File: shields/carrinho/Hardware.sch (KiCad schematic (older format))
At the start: 78 parts, among them J1 Conn_02x02_Odd_Even, J10 Conn_01x04, J11 Conn_01x04, J12 Conn_02x13_Odd_Even, J2 Conn_01x04, J3 Conn_02x02_Odd_Even, J4 Conn_01x02_Male, J5 Conn_01x02_Male, J6 Conn_01x02_Male, J7 Conn_01x02_Male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

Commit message: Improved schematic
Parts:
- C3: value C -> 100n
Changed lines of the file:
@@
 EESchema Schematic File Version 4
 LIBS:Hardware-cache
-EELAYER 30 0
+EELAYER 26 0
 EELAYER END
 $Descr A4 11693 8268
@@
 U 1 1 5CBBCEEC
 P 1300 5500
-F 0 "R14" H 1093 5500 50  0000 C CNN
-F 1 "15k" V 1184 5500 50  0000 C CNN
+F 0 "R14" V 1500 5500 50  0000 C CNN
+F 1 "15k" V 1400 5500 50  0000 C CNN
 F 2 "Resistor_SMD:R_0805_2012Metric" V 1230 5500 50  0001 C CNN
 F 3 "~" H 1300 5500 50  0001 C CNN
@@
 P 1300 5300
 F 0 "R12" V 1093 5300 50  0000 C CNN
-F 1 "15k" V 1184 5300 50  0000 C CNN
+F 1 "15k" V 1200 5300 50  0000 C CNN
 F 2 "Resistor_SMD:R_0805_2012Metric" V 1230 5300 50  0001 C CNN
 F 3 "~" H 1300 5300 50  0001 C CNN
@@
 P 3050 5400
 F 0 "#PWR017" H 3050 5250 50  0001 C CNN
-F 1 "+BATT" H 3065 5573 50  0000 C CNN
+F 1 "+BATT" H 2900 5350 50  0000 C CNN
 F 2 "" H 3050 5400 50  0001 C CNN
 F 3 "" H 3050 5400 50  0001 C CNN
@@
 U 1 1 5CC0410F
 P 3200 5450
-F 0 "R13" H 2993 5450 50  0000 C CNN
-F 1 "30k" V 3084 5450 50  0000 C CNN
+F 0 "R13" V 3400 5450 50  0000 C CNN
+F 1 "30k" V 3300 5450 50  0000 C CNN
 F 2 "Resistor_SMD:R_0805_2012Metric" V 3130 5450 50  0001 C CNN
 F 3 "~" H 3200 5450 50  0001 C CNN
@@
 U 1 1 5CC04116
 P 3200 5250
-F 0 "R11" V 2993 5250 50  0000 C CNN
-F 1 "30k" V 3084 5250 50  0000 C CNN
+F 0 "R11" V 3000 5250 50  0000 C CNN
+F 1 "30k" V 3100 5250 50  0000 C CNN
 F 2 "Resistor_SMD:R_0805_2012Metric" V 3130 5250 50  0001 C CNN
 F 3 "~" H 3200 5250 50  0001 C CNN
@@
 Text Notes 6500 2650 0    79   ~ 0
 Ponte H Lado esquerdo\n
-Text Notes 800  4700 0    79   ~ 0
+Text Notes 800  4650 0    79   ~ 0
 Diferencial bateria
 Wire Notes Line
@@
 U 1 1 5CE81B2B
 P 8900 5650
-F 0 "RV2" H 8830 5696 50  0000 R CNN
-F 1 "R_POT_TRIM" H 8830 5605 50  0000 R CNN
+F 0 "RV2" H 8800 5550 50  0000 R CNN
+F 1 "R_POT_TRIM" H 8800 5450 50  0000 R CNN
 F 2 "Potentiometer_THT:Potentiometer_Piher_PT-10-H01_Horizontal" H 8900 5650 50  0001 C CNN
 F 3 "~" H 8900 5650 50  0001 C CNN
@@
 U 2 1 5CF27E4C
 P 10250 5550
-F 0 "U1" H 10250 5917 50  0000 C CNN
-F 1 "LM393" H 10250 5826 50  0000 C CNN
+F 0 "U1" H 10150 5900 50  0000 C CNN
+F 1 "LM393" H 10200 5800 50  0000 C CNN
 F 2 "" H 10250 5550 50  0001 C CNN
 F 3 "http://www.ti.com/lit/ds/symlink/lm393-n.pdf" H 10250 5550 50  0001 C CNN
@@
 U 1 1 5CF855F3
 P 10650 5250
-F 0 "D10" V 10688 5133 50  0000 R CNN
+F 0 "D10" V 10700 5100 50  0000 R CNN
 F 1 "LED" V 10597 5133 50  0000 R CNN
 F 2 "LED_SMD:LED_0805_2012Metric" H 10650 5250 50  0001 C CNN
@@
 U 1 1 5CFF8CA7
 P 6550 5650
-F 0 "RV1" H 6480 5696 50  0000 R CNN
-F 1 "R_POT_TRIM" H 6480 5605 50  0000 R CNN
+F 0 "RV1" H 6450 5600 50  0000 R CNN
+F 1 "R_POT_TRIM" H 6500 5450 50  0000 R CNN
 F 2 "Potentiometer_THT:Potentiometer_Piher_PT-10-H01_Horizontal" H 6550 5650 50  0001 C CNN
 F 3 "~" H 6550 5650 50  0001 C CNN
@@
 U 3 1 5D0103DD
 P 6050 5500
-F 0 "U1" H 6008 5546 50  0000 L CNN
-F 1 "LM393" H 6008 5455 50  0000 L CNN
+F 0 "U1" H 5700 5600 50  0000 L CNN
+F 1 "LM393" H 5650 5500 50  0000 L CNN
 F 2 "" H 6050 5500 50  0001 C CNN
 F 3 "http://www.ti.com/lit/ds/symlink/lm393-n.pdf" H 6050 5500 50  0001 C CNN
@@
 	11100 4500 5800 4500
 Wire Notes Line
-	5800 4500 5800 6450
-Wire Notes Line
-	5800 6450 11100 6450
+	5650 4500 5650 6450
+Wire Notes Line
+	5650 6450 10950 6450
 Wire Notes Line
 	11100 6450 11100 4500
@@
 U 1 1 5D4E9A1A
 P 10550 5250
-F 0 "R34" H 10620 5296 50  0000 L CNN
-F 1 "10k" H 10620 5205 50  0000 L CNN
+F 0 "R34" H 10350 5400 50  0000 L CNN
+F 1 "10k" H 10350 5300 50  0000 L CNN
 F 2 "Resistor_SMD:R_0805_2012Metric_Pad1.15x1.40mm_HandSolder" V 10480 5250 50  0001 C CNN
 F 3 "~" H 10550 5250 50  0001 C CNN
@@
 U 1 1 5CBB5DEC
 P 1900 5400
-F 0 "U3" H 1900 5033 50  0000 C CNN
-F 1 "LM324" H 1900 5124 50  0000 C CNN
+F 0 "U3" H 1900 5100 50  0000 C CNN
+F 1 "LM324" H 1950 5200 50  0000 C CNN
 F 2 "Package_SO:SOIC-14_3.9x8.7mm_P1.27mm" H 1850 5500 50  0001 C CNN
 F 3 "http://www.ti.com/lit/ds/symlink/lm2902-n.pdf" H 1950 5600 50  0001 C CNN
@@
 P 6150 5500
 F 0 "C3" H 6265 5546 50  0000 L CNN
-F 1 "C" H 6265 5455 50  0000 L CNN
+F 1 "100n" H 6265 5455 50  0000 L CNN
 F 2 "Capacitor_SMD:C_0805_2012Metric" H 6188 5350 50  0001 C CNN
 F 3 "~" H 6150 5500 50  0001 C CNN

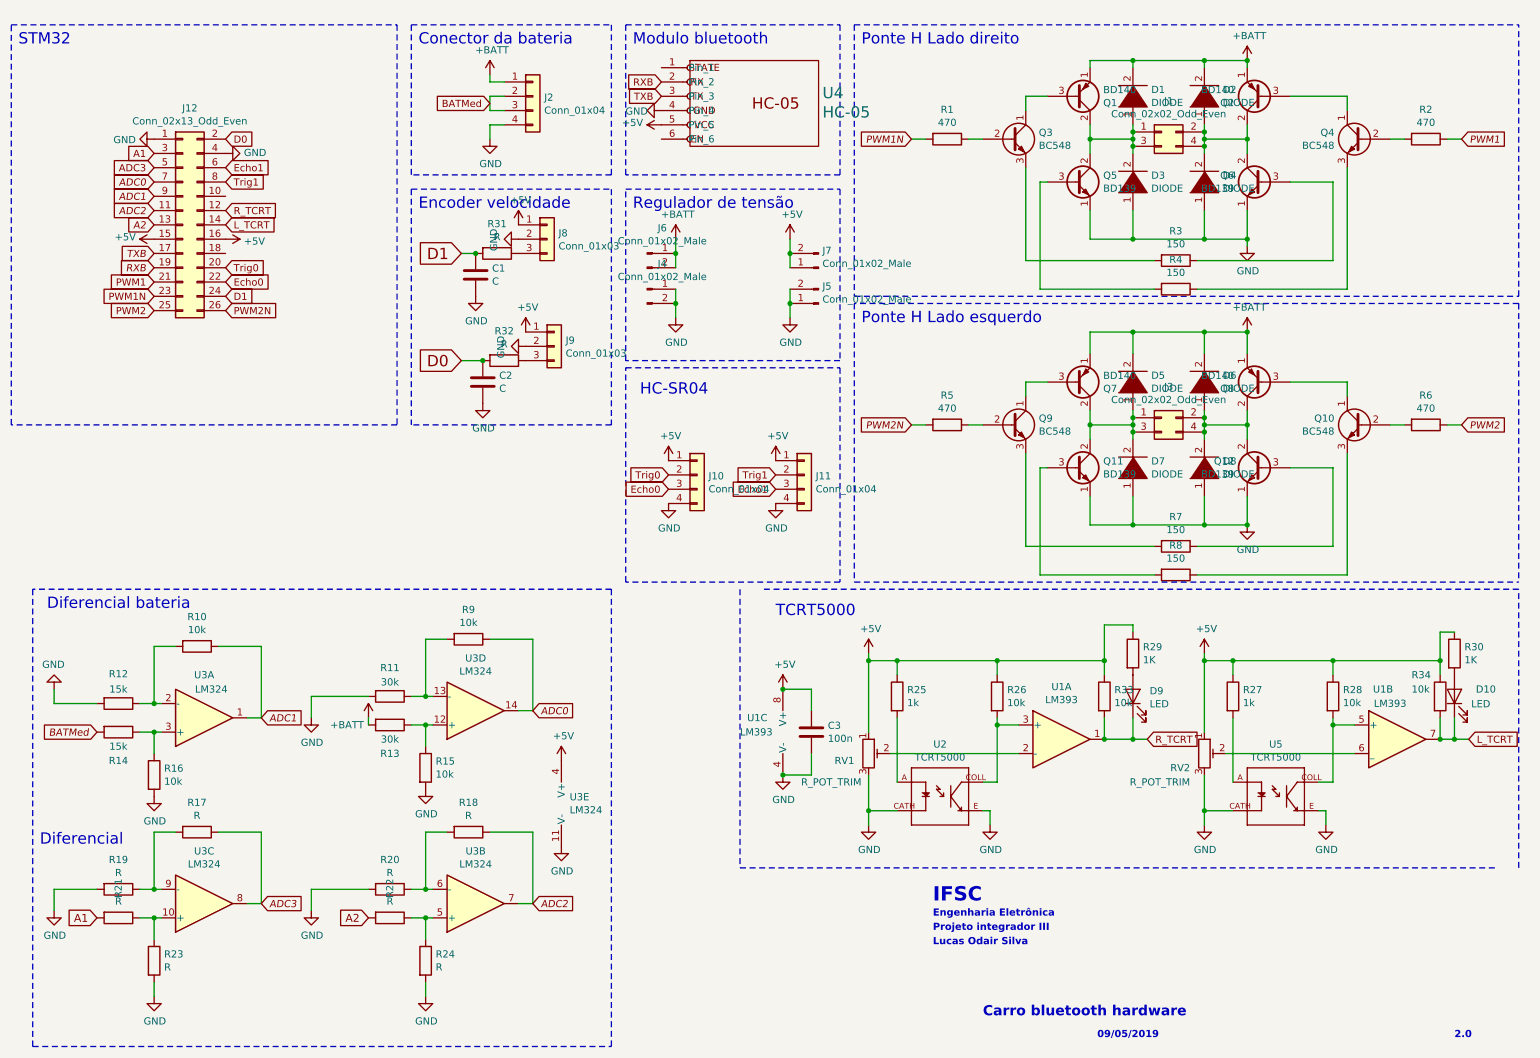
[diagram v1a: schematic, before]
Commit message: Changed motors conector, added capacitor near ampop
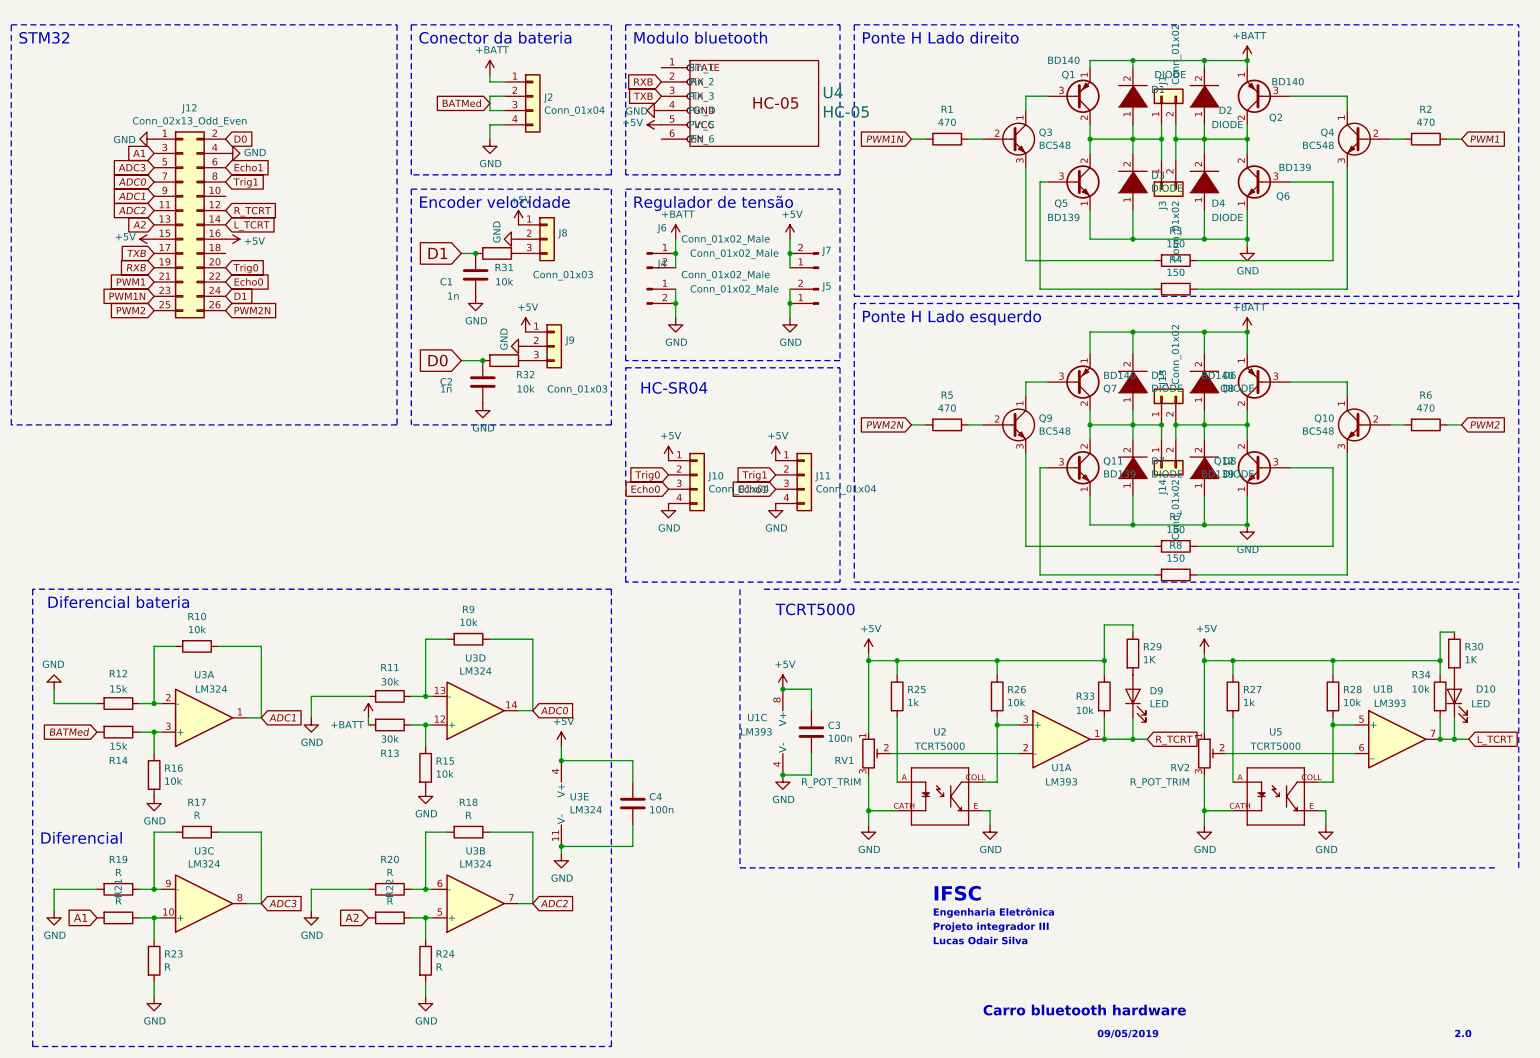
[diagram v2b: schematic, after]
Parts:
- removed J1, J3: Conn_02x02_Odd_Even, Connector_PinHeader_2.54mm:PinHeader_2x02_P2.54mm_Vertical, symbol Connector_Generic:Conn_02x02_Odd_Even
- added C4: 100n, Capacitor_SMD:C_0805_2012Metric, symbol Device:C
- added J1, J13, J14, J3: Conn_01x02, Connector_PinHeader_2.54mm:PinHeader_1x02_P2.54mm_Vertical, symbol Connector_Generic:Conn_01x02
- C1, C2: value C -> 1n
- R31, R32: value R -> 10k
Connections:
- net +5V: now also C4.1
- net GND: now also C4.2
- net at D1.1 (K), D3.2 (A), Q1.2 (C)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: now also J1.1 (Pin_1), J3.1 (Pin_1)
- net at D2.1 (K), D4.2 (A), Q2.2 (C)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: now also J1.2 (Pin_2), J3.2 (Pin_2)
- net at D5.1 (K), D7.2 (A), Q11.2 (C)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: now also J13.1 (Pin_1), J14.1 (Pin_1)
- net at D6.1 (K), D8.2 (A), Q12.2 (C)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: now also J13.2 (Pin_2), J14.2 (Pin_2)

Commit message: Changed pots
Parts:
- RV1, RV2: footprint Potentiometer_THT:Potentiometer_Piher_PT-10-H01_Horizontal -> Potentiometer_THT:Potentiometer_Piher_PT-6-V_Vertical
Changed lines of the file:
@@
 F 0 "RV2" H 8800 5550 50  0000 R CNN
 F 1 "R_POT_TRIM" H 8800 5450 50  0000 R CNN
-F 2 "Potentiometer_THT:Potentiometer_Piher_PT-10-H01_Horizontal" H 8900 5650 50  0001 C CNN
+F 2 "Potentiometer_THT:Potentiometer_Piher_PT-6-V_Vertical" H 8900 5650 50  0001 C CNN
 F 3 "~" H 8900 5650 50  0001 C CNN
 	1    8900 5650
@@
 F 0 "RV1" H 6450 5600 50  0000 R CNN
 F 1 "R_POT_TRIM" H 6500 5450 50  0000 R CNN
-F 2 "Potentiometer_THT:Potentiometer_Piher_PT-10-H01_Horizontal" H 6550 5650 50  0001 C CNN
+F 2 "Potentiometer_THT:Potentiometer_Piher_PT-6-V_Vertical" H 6550 5650 50  0001 C CNN
 F 3 "~" H 6550 5650 50  0001 C CNN
 	1    6550 5650

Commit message: Updated car PCB
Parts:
- added D11: LED, LED_SMD:LED_0805_2012Metric, symbol Device:LED
- added D12: D_Schottky, Diode_SMD:D_SMB, symbol Device:D_Schottky
- added H1, H2, H3: MountingHole, MountingHole:MountingHole_3.2mm_M3, symbol Mechanical:MountingHole
- added R35: 1K, Resistor_SMD:R_0805_2012Metric, symbol Device:R
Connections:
- net +5V: now also D11.2 (A)
- net +BATT: now also D12.1 (K); no longer J2.1 (Pin_1)
- net GND: now also R35.2
- new net: D12.2 (A), J2.1 (Pin_1)
- new net: D11.1 (K), R35.1
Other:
- note added: "Controll conector"
- note removed: "STM32"
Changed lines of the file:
@@
 L power:+BATT #PWR06
 U 1 1 5CBAF568
-P 3900 900
-F 0 "#PWR06" H 3900 750 50  0001 C CNN
-F 1 "+BATT" H 3915 1073 50  0000 C CNN
-F 2 "" H 3900 900 50  0001 C CNN
-F 3 "" H 3900 900 50  0001 C CNN
-	1    3900 900
-	1    0    0    -1
-$EndComp
-Wire Wire Line
-	3900 900  3900 950
-Wire Wire Line
-	3900 950  4000 950
+P 3450 950
+F 0 "#PWR06" H 3450 800 50  0001 C CNN
+F 1 "+BATT" H 3465 1123 50  0000 C CNN
+F 2 "" H 3450 950 50  0001 C CNN
+F 3 "" H 3450 950 50  0001 C CNN
+	1    3450 950
+	1    0    0    -1
+$EndComp
 Wire Wire Line
 	4000 1050 3900 1050
@@
 Wire Notes Line
 	4850 1700 6350 1700
-Text Notes 4900 1850 0    79   ~ 0
+Text Notes 4950 1850 0    79   ~ 0
 Regulador de tensão
 Wire Notes Line
@@
 	550  550  3250 550
 Text Notes 600  700  0    79   ~ 0
-STM32
+Controll conector
 $Comp
 L power:+5V #PWR0101
@@
 L power:+BATT #PWR02
 U 1 1 5CC49D66
-P 5200 2050
-F 0 "#PWR02" H 5200 1900 50  0001 C CNN
-F 1 "+BATT" H 5215 2223 50  0000 C CNN
-F 2 "" H 5200 2050 50  0001 C CNN
-F 3 "" H 5200 2050 50  0001 C CNN
-	1    5200 2050
+P 5200 2000
+F 0 "#PWR02" H 5200 1850 50  0001 C CNN
+F 1 "+BATT" H 5050 2050 50  0000 C CNN
+F 2 "" H 5200 2000 50  0001 C CNN
+F 3 "" H 5200 2000 50  0001 C CNN
+	1    5200 2000
 	1    0    0    -1
 $EndComp
@@
 U 1 1 5CEE1749
 P 5000 2400
-F 0 "J4" H 5106 2578 50  0000 C CNN
-F 1 "Conn_01x02_Male" H 5550 2500 50  0000 C CNN
+F 0 "J4" H 5000 2200 50  0000 C CNN
+F 1 "Conn_01x02_Male" H 5550 2100 50  0000 C CNN
 F 2 "Connector_PinSocket_2.54mm:PinSocket_1x02_P2.54mm_Vertical" H 5000 2400 50  0001 C CNN
 F 3 "~" H 5000 2400 50  0001 C CNN
@@
 P 6200 2500
 F 0 "J5" H 6173 2380 50  0000 R CNN
-F 1 "Conn_01x02_Male" H 7100 2400 50  0000 R CNN
+F 1 "Conn_01x02_Male" H 7100 2800 50  0000 R CNN
 F 2 "Connector_PinSocket_2.54mm:PinSocket_1x02_P2.54mm_Vertical" H 6200 2500 50  0001 C CNN
 F 3 "~" H 6200 2500 50  0001 C CNN
@@
 U 1 1 5CF103AE
 P 5000 2150
-F 0 "J6" H 5106 2328 50  0000 C CNN
-F 1 "Conn_01x02_Male" H 5550 2250 50  0000 C CNN
+F 0 "J6" H 4950 2150 50  0000 C CNN
+F 1 "Conn_01x02_Male" H 5600 1950 50  0000 C CNN
 F 2 "Connector_PinSocket_2.54mm:PinSocket_1x02_P2.54mm_Vertical" H 5000 2150 50  0001 C CNN
 F 3 "~" H 5000 2150 50  0001 C CNN
@@
 P 6200 2250
 F 0 "J7" H 6173 2130 50  0000 R CNN
-F 1 "Conn_01x02_Male" H 7100 2150 50  0000 R CNN
+F 1 "Conn_01x02_Male" H 7100 2400 50  0000 R CNN
 F 2 "Connector_PinSocket_2.54mm:PinSocket_1x02_P2.54mm_Vertical" H 6200 2250 50  0001 C CNN
 F 3 "~" H 6200 2250 50  0001 C CNN
@@
 	6000 2050 6000 2150
 Wire Wire Line
-	5200 2050 5200 2150
-Wire Wire Line
 	5200 2500 5200 2600
 $Comp
@@
 	8600 1500 8600 1350
 Connection ~ 8600 1350
+$Comp
+L Mechanical:MountingHole H1
+U 1 1 5D89937E
+P 850 3550
+F 0 "H1" H 950 3596 50  0000 L CNN
+F 1 "MountingHole" H 950 3505 50  0000 L CNN
+F 2 "MountingHole:MountingHole_3.2mm_M3" H 850 3550 50  0001 C CNN
+F 3 "~" H 850 3550 50  0001 C CNN
+	1    850  3550
+	1    0    0    -1
+$EndComp
+$Comp
+L Mechanical:MountingHole H2
+U 1 1 5D8995E4
+P 850 3850
+F 0 "H2" H 950 3896 50  0000 L CNN
+F 1 "MountingHole" H 950 3805 50  0000 L CNN
+F 2 "MountingHole:MountingHole_3.2mm_M3" H 850 3850 50  0001 C CNN
+F 3 "~" H 850 3850 50  0001 C CNN
+	1    850  3850
+	1    0    0    -1
+$EndComp
+$Comp
+L Mechanical:MountingHole H3
+U 1 1 5D899751
+P 1750 3550
+F 0 "H3" H 1850 3596 50  0000 L CNN
+F 1 "MountingHole" H 1850 3505 50  0000 L CNN
+F 2 "MountingHole:MountingHole_3.2mm_M3" H 1750 3550 50  0001 C CNN
+F 3 "~" H 1750 3550 50  0001 C CNN
+	1    1750 3550
+	1    0    0    -1
+$EndComp
+$Comp
+L Device:D_Schottky D12
+U 1 1 5D89B26A
+P 3800 950
+F 0 "D12" H 3800 1050 50  0000 C CNN
+F 1 "D_Schottky" H 4100 1100 50  0000 C CNN
+F 2 "Diode_SMD:D_SMB" H 3800 950 50  0001 C CNN
+F 3 "~" H 3800 950 50  0001 C CNN
+	1    3800 950
+	1    0    0    -1
+$EndComp
+$Comp
+L Device:R R35
+U 1 1 5D8B9C61
+P 2950 2800
+F 0 "R35" H 3020 2846 50  0000 L CNN
+F 1 "1K" H 3020 2755 50  0000 L CNN
+F 2 "Resistor_SMD:R_0805_2012Metric" V 2880 2800 50  0001 C CNN
+F 3 "~" H 2950 2800 50  0001 C CNN
+	1    2950 2800
+	1    0    0    -1
+$EndComp
+$Comp
+L Device:LED D11
+U 1 1 5D8B9D9D
+P 2950 2450
+F 0 "D11" V 2988 2333 50  0000 R CNN
+F 1 "LED" V 2897 2333 50  0000 R CNN
+F 2 "LED_SMD:LED_0805_2012Metric" H 2950 2450 50  0001 C CNN
+F 3 "~" H 2950 2450 50  0001 C CNN
+	1    2950 2450
+	0    -1   -1   0
+$EndComp
+$Comp
+L power:GND #PWR09
+U 1 1 5D8B9EDF
+P 2950 3000
+F 0 "#PWR09" H 2950 2750 50  0001 C CNN
+F 1 "GND" H 2955 2827 50  0000 C CNN
+F 2 "" H 2950 3000 50  0001 C CNN
+F 3 "" H 2950 3000 50  0001 C CNN
+	1    2950 3000
+	1    0    0    -1
+$EndComp
+Wire Wire Line
+	2950 2950 2950 3000
+Wire Wire Line
+	2950 2600 2950 2650
+$Comp
+L power:+5V #PWR07
+U 1 1 5D91421D
+P 2950 2300
+F 0 "#PWR07" H 2950 2150 50  0001 C CNN
+F 1 "+5V" H 2965 2473 50  0000 C CNN
+F 2 "" H 2950 2300 50  0001 C CNN
+F 3 "" H 2950 2300 50  0001 C CNN
+	1    2950 2300
+	1    0    0    -1
+$EndComp
+Wire Wire Line
+	5200 2000 5200 2150
+Wire Wire Line
+	3950 950  4000 950
+Wire Wire Line
+	3650 950  3450 950
 $EndSCHEMATC

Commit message: Adicionado exmplos com IRQ da USART.
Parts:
- D1, D2, D3, D4, D5, D6, D7, D8: footprint Diode_THT:D_A-405_P2.54mm_Vertical_AnodeUp -> Diode_THT:D_A-405_P2.54mm_Vertical_KathodeUp
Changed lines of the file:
@@
 F 0 "D7" V 8446 3522 50  0000 R CNN
 F 1 "DIODE" V 8355 3522 50  0000 R CNN
-F 2 "Diode_THT:D_A-405_P2.54mm_Vertical_AnodeUp" H 8400 3650 50  0001 C CNN
+F 2 "Diode_THT:D_A-405_P2.54mm_Vertical_KathodeUp" H 8400 3650 50  0001 C CNN
 F 3 "~" H 8400 3650 50  0001 C CNN
 	1    8400 3650
@@
 F 0 "D3" V 8446 1522 50  0000 R CNN
 F 1 "DIODE" V 8355 1522 50  0000 R CNN
-F 2 "Diode_THT:D_A-405_P2.54mm_Vertical_AnodeUp" H 8400 1650 50  0001 C CNN
+F 2 "Diode_THT:D_A-405_P2.54mm_Vertical_KathodeUp" H 8400 1650 50  0001 C CNN
 F 3 "~" H 8400 1650 50  0001 C CNN
 	1    8400 1650
@@
 F 0 "D4" V 8750 1600 50  0000 R CNN
 F 1 "DIODE" V 8650 1600 50  0000 R CNN
-F 2 "Diode_THT:D_A-405_P2.54mm_Vertical_AnodeUp" H 8900 1650 50  0001 C CNN
+F 2 "Diode_THT:D_A-405_P2.54mm_Vertical_KathodeUp" H 8900 1650 50  0001 C CNN
 F 3 "~" H 8900 1650 50  0001 C CNN
 	1    8900 1650
@@
 F 0 "D2" V 8800 950 50  0000 R CNN
 F 1 "DIODE" V 8700 1000 50  0000 R CNN
-F 2 "Diode_THT:D_A-405_P2.54mm_Vertical_AnodeUp" H 8900 1050 50  0001 C CNN
+F 2 "Diode_THT:D_A-405_P2.54mm_Vertical_KathodeUp" H 8900 1050 50  0001 C CNN
 F 3 "~" H 8900 1050 50  0001 C CNN
 	1    8900 1050
@@
 F 0 "D1" V 8446 922 50  0000 R CNN
 F 1 "DIODE" V 8550 900 50  0000 R CNN
-F 2 "Diode_THT:D_A-405_P2.54mm_Vertical_AnodeUp" H 8400 1050 50  0001 C CNN
+F 2 "Diode_THT:D_A-405_P2.54mm_Vertical_KathodeUp" H 8400 1050 50  0001 C CNN
 F 3 "~" H 8400 1050 50  0001 C CNN
 	1    8400 1050
@@
 F 0 "D5" V 8446 2922 50  0000 R CNN
 F 1 "DIODE" V 8355 2922 50  0000 R CNN
-F 2 "Diode_THT:D_A-405_P2.54mm_Vertical_AnodeUp" H 8400 3050 50  0001 C CNN
+F 2 "Diode_THT:D_A-405_P2.54mm_Vertical_KathodeUp" H 8400 3050 50  0001 C CNN
 F 3 "~" H 8400 3050 50  0001 C CNN
 	1    8400 3050
@@
 F 0 "D6" V 8946 2922 50  0000 R CNN
 F 1 "DIODE" V 8855 2922 50  0000 R CNN
-F 2 "Diode_THT:D_A-405_P2.54mm_Vertical_AnodeUp" H 8900 3050 50  0001 C CNN
+F 2 "Diode_THT:D_A-405_P2.54mm_Vertical_KathodeUp" H 8900 3050 50  0001 C CNN
 F 3 "~" H 8900 3050 50  0001 C CNN
 	1    8900 3050
@@
 F 0 "D8" V 8946 3522 50  0000 R CNN
 F 1 "DIODE" V 8855 3522 50  0000 R CNN
-F 2 "Diode_THT:D_A-405_P2.54mm_Vertical_AnodeUp" H 8900 3650 50  0001 C CNN
+F 2 "Diode_THT:D_A-405_P2.54mm_Vertical_KathodeUp" H 8900 3650 50  0001 C CNN
 F 3 "~" H 8900 3650 50  0001 C CNN
 	1    8900 3650
